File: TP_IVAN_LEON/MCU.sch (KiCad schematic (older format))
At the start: 21 parts, among them P3 CONN_01X06, P4 POWER_OUT, P5 ANALOG_IN, U2 32.768HZ, U3 12MHZ, U4 LPC1769FBD100

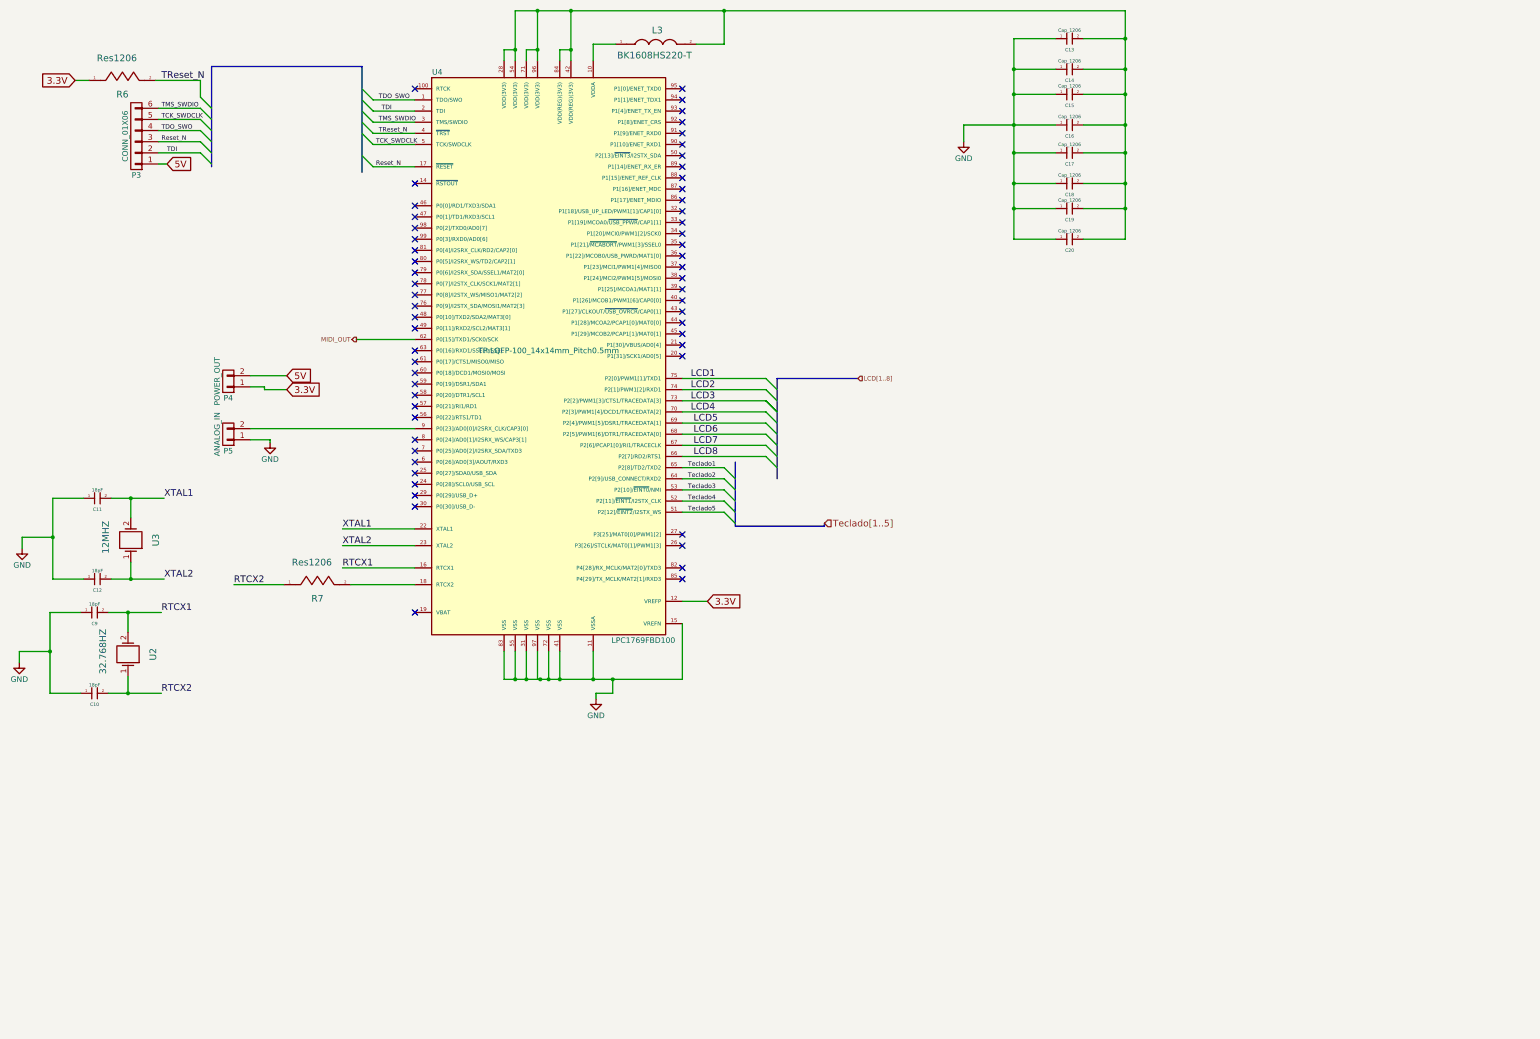
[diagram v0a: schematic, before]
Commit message: Agregado codigo digey key en 80% de componentes
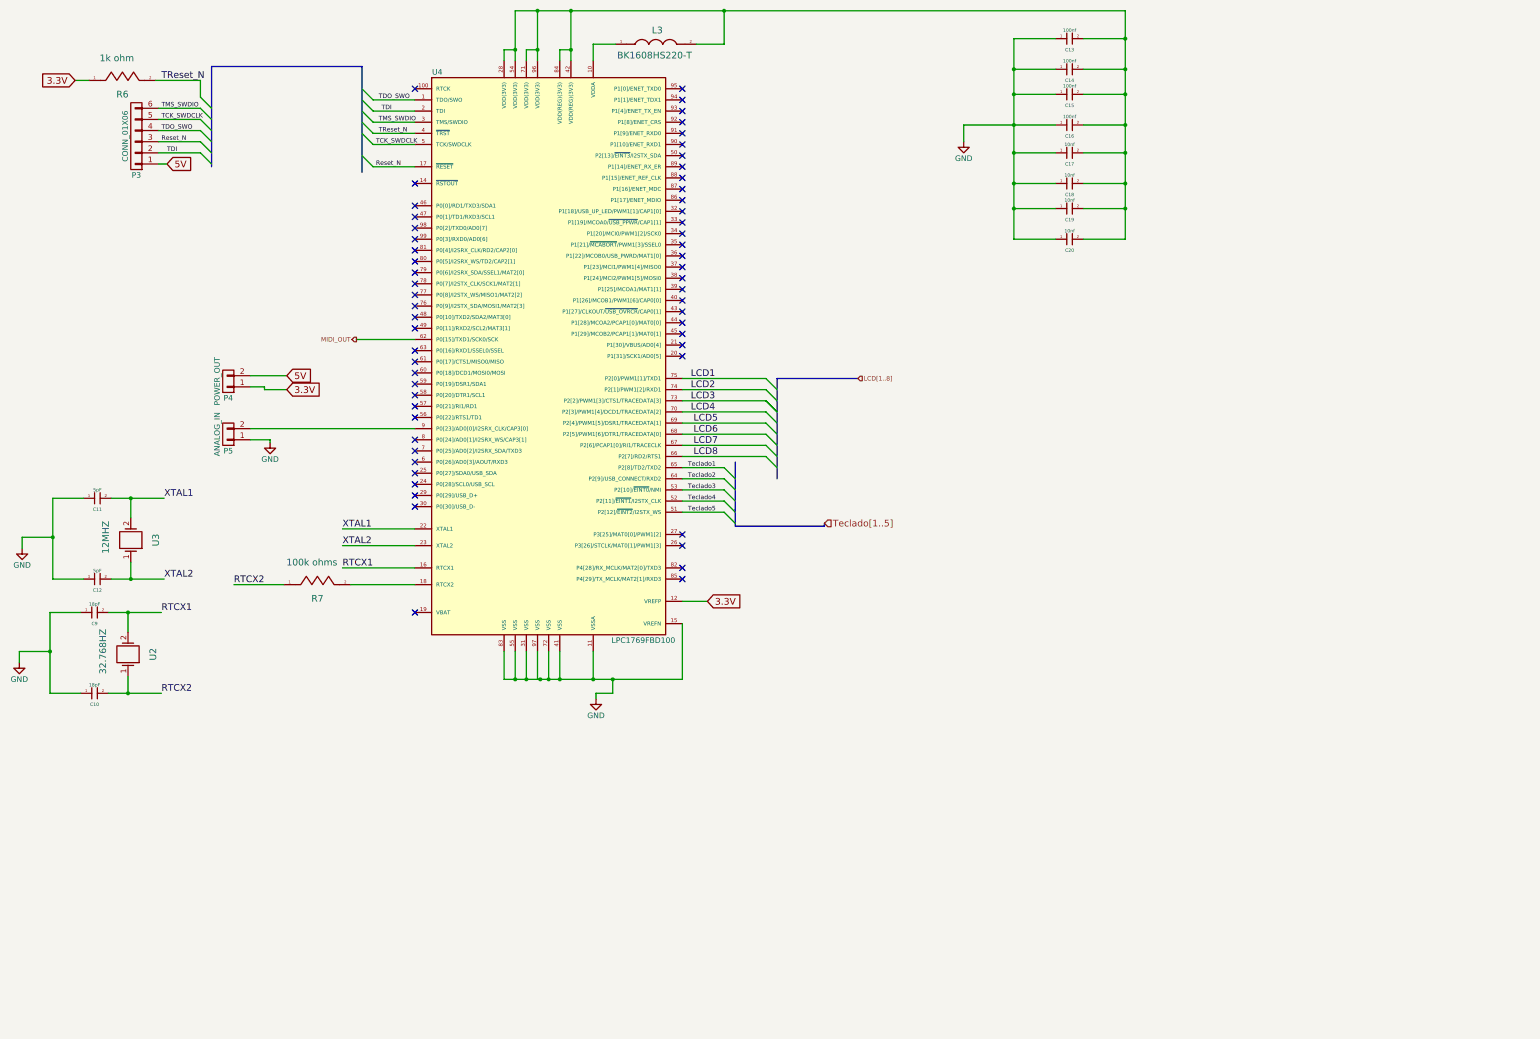
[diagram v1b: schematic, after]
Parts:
- C10, C9: Digikey# (none) -> C1206C180D5GACTU-ND
- C11, C12: value 18pF -> 5pF; Digikey# (none) -> 12061A5R0CAT2A-ND
- C13, C14, C15, C16: value Cap_1206 -> 100nf; Digikey# (none) -> 1276-1007-1-ND
- C17, C18, C19, C20: value Cap_1206 -> 10nf; Digikey# (none) -> 1276-2705-2-ND
- L3: Digikey# (none) -> 587-1869-2-ND
- P3: Digikey# (none) -> WM1735-ND
- P4, P5: Digikey# (none) -> WM1731-ND
- R6: value Res1206 -> 1k ohm; Digikey# (none) -> YAG1338TR-ND
- R7: value Res1206 -> 100k ohms; Digikey# (none) -> HVCB1206FKC100KTR-ND
- U2: Digikey# (none) -> CFS-20632768HZBB-ND
- U3: Digikey# (none) -> X1037-ND
- U4: Digikey# (none) -> 568-4966-ND
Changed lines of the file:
@@
 F 0 "U4" H 4425 6450 50  0000 C CNN
 F 1 "LPC1769FBD100" H 6275 1350 50  0000 C CNN
-F 2 "TP:LQFP-100_14x14mm_Pitch0.5mm" H 5425 3950 50  0000 C CNN
+F 2 "TP:LQFP-100_14x14mm_Pitch0.5mm" H 5425 3950 50  0001 C CNN
 F 3 "" H 5425 3950 50  0000 C CNN
+F 4 "568-4966-ND" H 5425 3950 60  0001 C CNN "Digikey#"
 	1    5425 3950
 	1    0    0    -1
@@
 P 1575 1525
 F 0 "R6" H 1600 1400 60  0000 C CNN
-F 1 "Res1206" H 1550 1725 60  0000 C CNN
+F 1 "1k ohm" H 1550 1725 60  0000 C CNN
 F 2 "TP:Resistor_SMD+THTuniversal_1206_RM10_HandSoldering" H 1575 1525 60  0001 C CNN
 F 3 "" H 1575 1525 60  0000 C CNN
+F 4 "YAG1338TR-ND" H 1575 1525 60  0001 C CNN "Digikey#"
 	1    1575 1525
 	1    0    0    -1
@@
 F 2 "TP:Crystal_HC49-U_Vertical" H 1725 5650 60  0001 C CNN
 F 3 "" H 1725 5650 60  0000 C CNN
+F 4 "X1037-ND" H 1675 5650 60  0001 C CNN "Digikey#"
 	1    1675 5650
 	0    -1   -1   0
@@
 P 1375 5275
 F 0 "C11" H 1375 5175 30  0000 C CNN
-F 1 "18pF" H 1375 5350 30  0000 C CNN
+F 1 "5pF" H 1375 5350 30  0000 C CNN
 F 2 "TP:C_0805_HandSoldering" H 1400 5275 60  0001 C CNN
 F 3 "" H 1400 5275 60  0000 C CNN
+F 4 "12061A5R0CAT2A-ND" H 1375 5275 60  0001 C CNN "Digikey#"
 	1    1375 5275
 	1    0    0    -1
@@
 P 1375 6000
 F 0 "C12" H 1375 5900 30  0000 C CNN
-F 1 "18pF" H 1375 6075 30  0000 C CNN
+F 1 "5pF" H 1375 6075 30  0000 C CNN
 F 2 "TP:C_0805_HandSoldering" H 1400 6000 60  0001 C CNN
 F 3 "" H 1400 6000 60  0000 C CNN
+F 4 "12061A5R0CAT2A-ND" H 1375 6000 60  0001 C CNN "Digikey#"
 	1    1375 6000
 	1    0    0    -1
@@
 F 2 "TP:Crystal_HC49-U_Vertical" H 1700 6675 60  0001 C CNN
 F 3 "" H 1700 6675 60  0000 C CNN
+F 4 "CFS-20632768HZBB-ND" H 1650 6675 60  0001 C CNN "Digikey#"
 	1    1650 6675
 	0    -1   -1   0
@@
 F 2 "TP:C_0805_HandSoldering" H 1375 6300 60  0001 C CNN
 F 3 "" H 1375 6300 60  0000 C CNN
+F 4 "C1206C180D5GACTU-ND" H 1350 6300 60  0001 C CNN "Digikey#"
 	1    1350 6300
 	1    0    0    -1
@@
 F 2 "TP:C_0805_HandSoldering" H 1375 7025 60  0001 C CNN
 F 3 "" H 1375 7025 60  0000 C CNN
+F 4 "C1206C180D5GACTU-ND" H 1350 7025 60  0001 C CNN "Digikey#"
 	1    1350 7025
 	1    0    0    -1
@@
 P 10100 1150
 F 0 "C13" H 10100 1050 30  0000 C CNN
-F 1 "Cap_1206" H 10100 1225 30  0000 C CNN
+F 1 "100nf" H 10100 1225 30  0000 C CNN
 F 2 "TP:c_1206" H 10125 1150 60  0001 C CNN
 F 3 "" H 10125 1150 60  0000 C CNN
+F 4 "1276-1007-1-ND" H 10100 1150 60  0001 C CNN "Digikey#"
 	1    10100 1150
 	1    0    0    -1
@@
 P 10100 1425
 F 0 "C14" H 10100 1325 30  0000 C CNN
-F 1 "Cap_1206" H 10100 1500 30  0000 C CNN
+F 1 "100nf" H 10100 1500 30  0000 C CNN
 F 2 "TP:c_1206" H 10125 1425 60  0001 C CNN
 F 3 "" H 10125 1425 60  0000 C CNN
+F 4 "1276-1007-1-ND" H 10100 1425 60  0001 C CNN "Digikey#"
 	1    10100 1425
 	1    0    0    -1
@@
 P 10100 1650
 F 0 "C15" H 10100 1550 30  0000 C CNN
-F 1 "Cap_1206" H 10100 1725 30  0000 C CNN
+F 1 "100nf" H 10100 1725 30  0000 C CNN
 F 2 "TP:c_1206" H 10125 1650 60  0001 C CNN
 F 3 "" H 10125 1650 60  0000 C CNN
+F 4 "1276-1007-1-ND" H 10100 1650 60  0001 C CNN "Digikey#"
 	1    10100 1650
 	1    0    0    -1
@@
 P 10100 1925
 F 0 "C16" H 10100 1825 30  0000 C CNN
-F 1 "Cap_1206" H 10100 2000 30  0000 C CNN
+F 1 "100nf" H 10100 2000 30  0000 C CNN
 F 2 "TP:c_1206" H 10125 1925 60  0001 C CNN
 F 3 "" H 10125 1925 60  0000 C CNN
+F 4 "1276-1007-1-ND" H 10100 1925 60  0001 C CNN "Digikey#"
 	1    10100 1925
 	1    0    0    -1
@@
 P 10100 2175
 F 0 "C17" H 10100 2075 30  0000 C CNN
-F 1 "Cap_1206" H 10100 2250 30  0000 C CNN
+F 1 "10nf" H 10100 2250 30  0000 C CNN
 F 2 "TP:c_1206" H 10125 2175 60  0001 C CNN
 F 3 "" H 10125 2175 60  0000 C CNN
+F 4 "1276-2705-2-ND" H 10100 2175 60  0001 C CNN "Digikey#"
 	1    10100 2175
 	1    0    0    -1
@@
 P 10100 2450
 F 0 "C18" H 10100 2350 30  0000 C CNN
-F 1 "Cap_1206" H 10100 2525 30  0000 C CNN
+F 1 "10nf" H 10100 2525 30  0000 C CNN
 F 2 "TP:c_1206" H 10125 2450 60  0001 C CNN
 F 3 "" H 10125 2450 60  0000 C CNN
+F 4 "1276-2705-2-ND" H 10100 2450 60  0001 C CNN "Digikey#"
 	1    10100 2450
 	1    0    0    -1
@@
 P 10100 2675
 F 0 "C19" H 10100 2575 30  0000 C CNN
-F 1 "Cap_1206" H 10100 2750 30  0000 C CNN
+F 1 "10nf" H 10100 2750 30  0000 C CNN
 F 2 "TP:c_1206" H 10125 2675 60  0001 C CNN
 F 3 "" H 10125 2675 60  0000 C CNN
+F 4 "1276-2705-2-ND" H 10100 2675 60  0001 C CNN "Digikey#"
 	1    10100 2675
 	1    0    0    -1
@@
 P 10100 2950
 F 0 "C20" H 10100 2850 30  0000 C CNN
-F 1 "Cap_1206" H 10100 3025 30  0000 C CNN
+F 1 "10nf" H 10100 3025 30  0000 C CNN
 F 2 "TP:c_1206" H 10125 2950 60  0001 C CNN
 F 3 "" H 10125 2950 60  0000 C CNN
+F 4 "1276-2705-2-ND" H 10100 2950 60  0001 C CNN "Digikey#"
 	1    10100 2950
 	1    0    0    -1
@@
 F 2 "TP:Choke_SMD_1206_Standard" H 6375 1200 60  0001 C CNN
 F 3 "" H 6375 1200 60  0000 C CNN
+F 4 "587-1869-2-ND" H 6375 1200 60  0001 C CNN "Digikey#"
 	1    6375 1200
 	1    0    0    -1
@@
 F 2 "TP:Connector_Molex_PicoBlade_53047-0210" H 2550 4700 50  0001 C CNN
 F 3 "" H 2550 4700 50  0000 C CNN
+F 4 "WM1731-ND" H 2550 4700 60  0001 C CNN "Digikey#"
 	1    2550 4700
 	-1   0    0    1
@@
 F 2 "TP:Connector_Molex_PicoBlade_53047-0210" H 2550 4225 50  0001 C CNN
 F 3 "" H 2550 4225 50  0000 C CNN
+F 4 "WM1731-ND" H 2550 4225 60  0001 C CNN "Digikey#"
 	1    2550 4225
 	-1   0    0    1
@@
 F 2 "TP:Connector_Molex_PicoBlade_53047-0610" H 1725 2025 50  0001 C CNN
 F 3 "" H 1725 2025 50  0000 C CNN
+F 4 "WM1735-ND" H 1725 2025 60  0001 C CNN "Digikey#"
 	1    1725 2025
 	-1   0    0    1
@@
 P 3325 6050
 F 0 "R7" H 3350 5925 60  0000 C CNN
-F 1 "Res1206" H 3300 6250 60  0000 C CNN
+F 1 "100k ohms" H 3300 6250 60  0000 C CNN
 F 2 "TP:Resistor_SMD+THTuniversal_1206_RM10_HandSoldering" H 3325 6050 60  0001 C CNN
 F 3 "" H 3325 6050 60  0000 C CNN
+F 4 "HVCB1206FKC100KTR-ND" H 3325 6050 60  0001 C CNN "Digikey#"
 	1    3325 6050
 	1    0    0    -1

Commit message: Agregado cambios subrayados en verde descritos en documento Leonv.ods en la carpeta docs
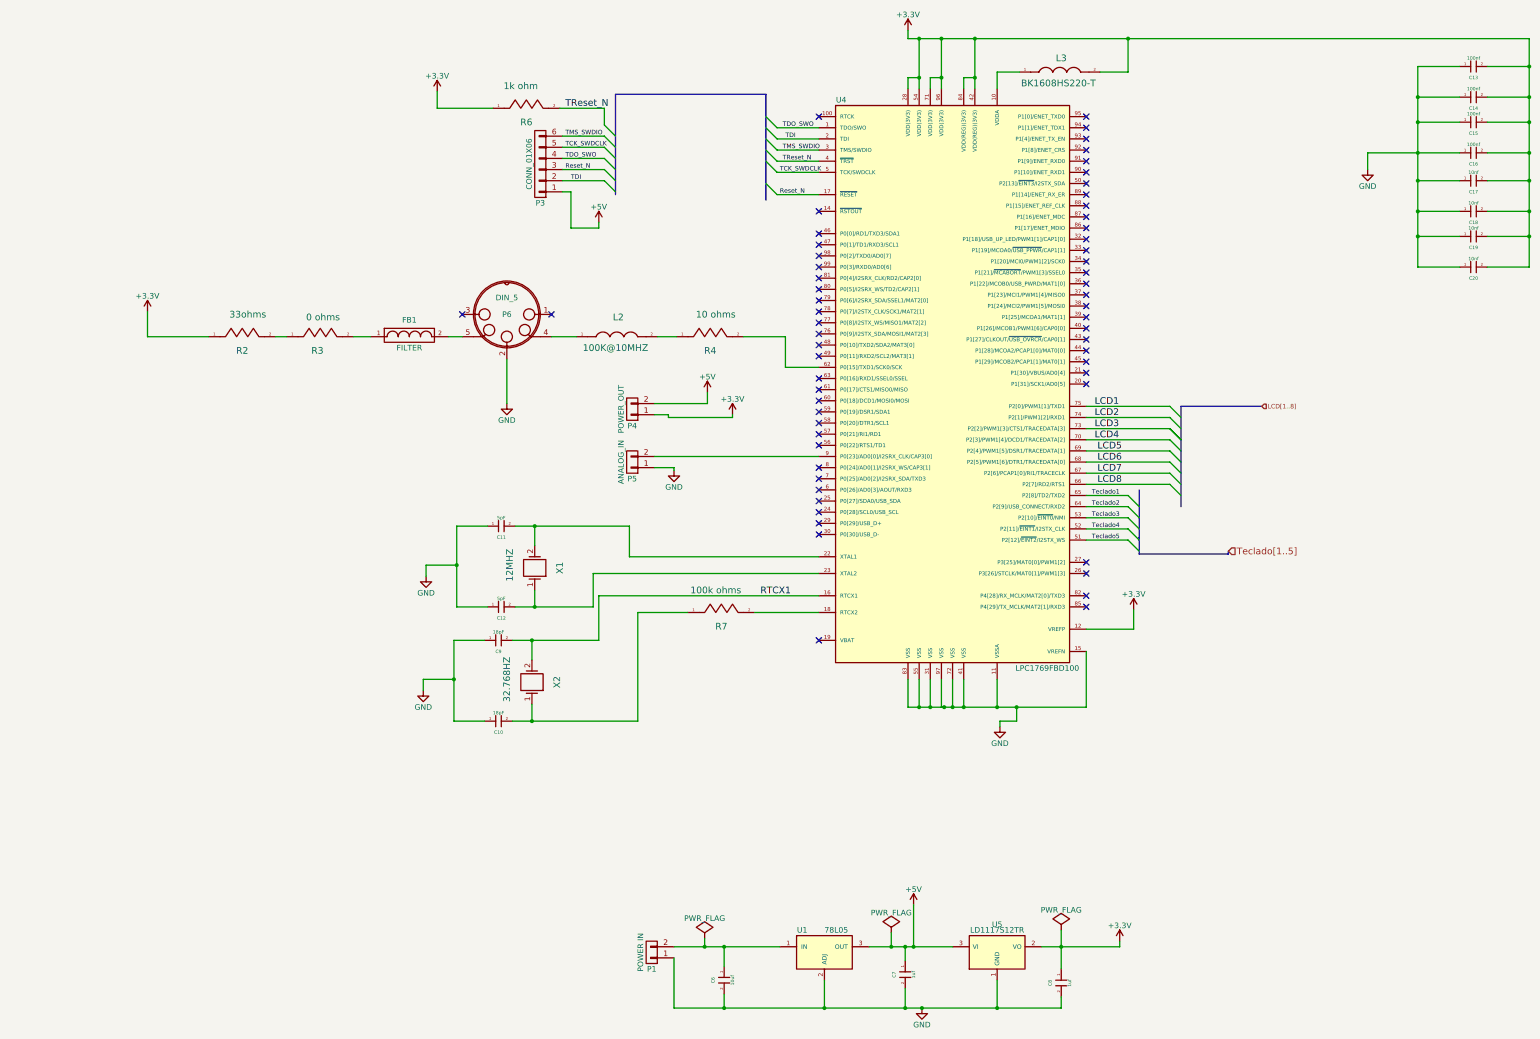
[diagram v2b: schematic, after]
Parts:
- added C6: 10uf, TP:c_1206, symbol Cap_1206
- added C7, C8: 1uf, TP:c_1206, symbol Cap_1206
- added FB1: FILTER, TP:Choke_SMD_1206_Standard, symbol FILTER
- added L2: 100K@10MHZ, TP:Choke_SMD_1206_Standard, symbol 100K@10MHZ
- added P1: POWER IN, TP:Connector_Molex_PicoBlade_53047-0210, symbol CONN_01X02
- added P6: DIN_5, TP:din-5, symbol DIN_5
- added R2: 33ohms, TP:Resistor_SMD+THTuniversal_1206_RM10_HandSoldering, symbol Res1206
- added R3: 0 ohms, TP:Resistor_SMD+THTuniversal_0805to2512_RM10_HandSoldering, symbol Res0805
- added R4: 10 ohms, TP:Resistor_SMD+THTuniversal_1206_RM10_HandSoldering, symbol Res1206
- added U1: 78L05, TP:SOT-223, symbol LM117H
- added U5: LD1117S12TR, TP:SOT-223, symbol LD1117S12TR
- renumbered U3 to X1, U2 to X2
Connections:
- net 3.3V is gone; now on net +3V3: P4.1 (P1), R6.1, U4.12 (VREFP)
- net GND: now also C6.2, C7.2, C8.2, P1.1 (P1), P6.2, U1.2 (ADJ), U5.1 (GND)
- net +3V3: now reaches C13.2, C14.2, C15.2, C16.2, C17.2, C18.2, C19.2, C20.2, L3.2, U4.28 (VDD(3V3)), U4.42 (VDD(REG)(3V3)), U4.54 (VDD(3V3)), U4.71 (VDD(3V3)), U4.84 (VDD(REG)(3V3)), U4.96 (VDD(3V3))
- net +3V3: now also C8.1, R2.1, U5.2 (VO)
- net 5V renamed +5V
- net +5V: now also C7.1, U1.3 (OUT), U5.3 (VI)
- net MIDI_OUT: no longer names the net of U4.62 (P0[15]/TXD1/SCK0/SCK)
- net MIDI_OUT: now also R4.2
- net RTCX2: no longer names the net of C10.2, R7.1, X2.1
- net XTAL1: no longer names the net of C11.2, U4.22 (XTAL1), X1.2
- net XTAL2: no longer names the net of C12.2, U4.23 (XTAL2), X1.1
- new net: C6.1, P1.2 (P2), U1.1 (IN)
- new net: L2.1, P6.4
- new net: L2.2, R4.1
- new net: R2.2, R3.1
- new net: FB1.1, R3.2
- new net: FB1.2, P6.5
- no-connect marks 58 -> 60
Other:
- moved on the sheet: C10, C11, C12, C13, C14, C15, C16, C17, C18, C19, C20, C9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
